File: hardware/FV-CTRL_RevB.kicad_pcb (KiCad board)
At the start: 2 copper layers, 100 x 100 mm, 152 parts, among them J1 12V INPUT, J10 IR RX2 3V3/OUT/G, J11 IR TX1 A/K, J12 IR TX2 A/K, J13 LS1 DNP, J14 LS2 DNP, J15 LS3 DNP, J16 LS4 DNP, J17 I2C 3V3/SDA/SCL/G, J2 XL4015 A: 12/G/6/G, J20 SMA 50ohm ANT, J21 USB MICRO DATA, J3 XL4015 B: 12/G/6/G, J4 5V D24V25F5, J5 S1_TOP, J6 S1_BOT, J7 S2_TOP, J8 S2_BOT, J9 IR RX1 3V3/OUT/G, Q1 IRF4905PBF, Q2 P2N2222AG, Q3 MMBT3904, Q4 MMBT3904, SW1 RESET, SW2 BOOT, U1 ESP32-D0WD-V3, U2 CP2102N-A02-GQFN24, U3 LD1117V33, U4 W25Q32JVSSIQ, U5 TLV803EA30DBZR, Y1 40MHz CL10pF

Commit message: feat(pcb): order QFN escapes and reconnect local supplies before signal routing
Keep two servo rails and GPIO unchanged. Use 0.4/0.2mm escape vias, move C23 to 0201 and preserve ground beneath clock/RF. ERC has zero violations; native DRC has no physical errors or parity differences, with 100 opens and 33 dangling warnings at this intermediate checkpoint. Not a fabrication release.
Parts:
- C23: footprint Capacitor_SMD:C_0402_1005Metric -> Capacitor_SMD:C_0201_0603Metric
- moved U5 10.0 mm to (135.0, 166.0)
- moved C56 4.47 mm to (138.0, 164.5)
- moved C13 4.29 mm to (142.0, 162.8), turned to -90 degrees
- moved C17 4.11 mm to (142.6, 159.8), turned to -90 degrees
- moved C18 2.77 mm to (149.0, 150.7), turned to 0 degrees
- moved C21 2.69 mm to (133.0, 157.5), turned to 90 degrees
- moved R40 2.50 mm to (150.5, 154.5)
- moved R41 2.50 mm to (150.5, 152.5)
- moved R42 2.50 mm to (152.5, 151.0)
- moved R43 2.50 mm to (154.5, 152.5)
- moved R44 2.50 mm to (152.5, 156.0)
- moved R45 2.50 mm to (150.5, 158.0)
- moved C15 2.00 mm to (135.5, 157.0), turned to 180 degrees
- moved C14 1.87 mm to (135.7, 154.0)
- moved C40 1.70 mm to (149.0, 156.8), turned to 0 degrees
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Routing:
- net +3V3: track 296.6 -> 350.2 mm, vias 9 -> 13
- net CAP2: track 0.00 -> 6.15 mm, vias 0 -> 2
- net CAP1: track 0.00 -> 4.27 mm, vias 0 -> 1
- net +3V3_RF: track 13.2 -> 16.8 mm
- net ESP_S2_BOT_PWM: track 0.00 -> 2.99 mm, vias 0 -> 1
- net ESP_S1_TOP_PWM: track 0.00 -> 2.99 mm, vias 0 -> 1
- net LS1: track 0.00 -> 2.90 mm, vias 0 -> 1
- net SPARE_GPIO33: track 0.00 -> 2.74 mm, vias 0 -> 1
- net ESP_IR_TX: track 0.00 -> 2.68 mm, vias 0 -> 1
- net ESP_S1_BOT_PWM: track 0.00 -> 2.68 mm, vias 0 -> 1
- net LS4: track 0.00 -> 2.62 mm, vias 0 -> 1
- net ESP_EN: track 0.00 -> 2.62 mm, vias 0 -> 1
- net IR_RX2: track 0.00 -> 2.56 mm, vias 0 -> 1
- net IR_RX1: track 0.00 -> 2.56 mm, vias 0 -> 1
- net SPI_HD: track 0.00 -> 2.56 mm, vias 0 -> 1
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
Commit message: feat(pcb): complete RevB routing, ground returns and service markings
Finish signal and supply connections, repair USB escape and C40 ground, and remove 24 redundant copper items. Apply 1mm/0.15mm silk rules, 0.025mm mask expansion and 0.10mm minimum mask web. Native KiCad ERC/DRC, opens and schematic parity are all zero. RF, thermal and hardware qualification remain pending; no Gerber release.
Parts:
- moved C40 4.57 mm to (145.0, 159.0), turned to 180 degrees
- moved C27 3.91 mm to (137.0, 146.0)
- moved C53 0.50 mm to (139.5, 183.8)
- moved C55 0.20 mm to (141.8, 188.4)
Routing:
- net LS2: track 2.08 -> 147.8 mm, vias 1 -> 10
- net LS3: track 1.89 -> 134.4 mm, vias 1 -> 0
- net LS1: track 2.90 -> 126.8 mm, vias 1 -> 10
- net LS4: track 2.62 -> 125.7 mm
- net I2C_SDA: track 1.78 -> 103.7 mm, vias 1 -> 3
- net I2C_SCL: track 2.14 -> 103.8 mm, vias 1 -> 2
- net ESP_EN: track 2.62 -> 102.0 mm, vias 1 -> 6
- net ESP_BOOT: track 1.84 -> 83.1 mm, vias 1 -> 4
- net UART_RX: track 1.99 -> 67.7 mm, vias 1 -> 4
- net ESP_IR_TX: track 2.68 -> 63.4 mm, vias 1 -> 2
- net IR_TX2_A: track 0.00 -> 58.8 mm
- net IR_TX_RET: track 0.00 -> 56.4 mm
- net IR_RX1: track 2.56 -> 58.8 mm, vias 1 -> 2
- net ESP_S2_BOT_PWM: track 2.99 -> 55.2 mm
- net UART_TX_RAW: track 1.86 -> 49.0 mm, vias 1 -> 6
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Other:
- rule pad_to_mask_clearance: 0 -> 0.025
- board text added: "12"
- board text added: "12V"
- board text added: "12V IN"
- board text added: "2026-10-20"
- board text added: "3V"
- board text added: "3V3"
- board text added: "5V"
- board text added: "5V LOGIC"
- board text added: "6A"
- board text added: "6B"
- board text added: "6V_A"
- board text added: "6V_B"
- board text added: "A"
- board text added: "ANT SMA"
- board text added: "BOOT"
- board text added: "BUCK A"
- board text added: "BUCK B"
- board text added: "EN"
- board text added: "FV-CTRL RevB"
- board text added: "G"
- board text added: "GND"
- board text added: "IO33"
- board text added: "J10 RX2"
- board text added: "J11 TX1"
- board text added: "J12 TX2"
- board text added: "J9 RX1"
- board text added: "K"
- board text added: "LS1 DNP"
- board text added: "LS2 DNP"
- board text added: "LS3 DNP"
- board text added: "LS4 DNP"
- board text added: "O"
- board text added: "RESET"
- board text added: "RX"
- board text added: "S"
- board text added: "S1 BOT"
- board text added: "S1 TOP"
- board text added: "S2 BOT"
- board text added: "S2 TOP"
- board text added: "SCL"
- board text added: "SDA"
- board text added: "TX"
- board text added: "USB DATA"
- board text added: "USB: 12V ON"

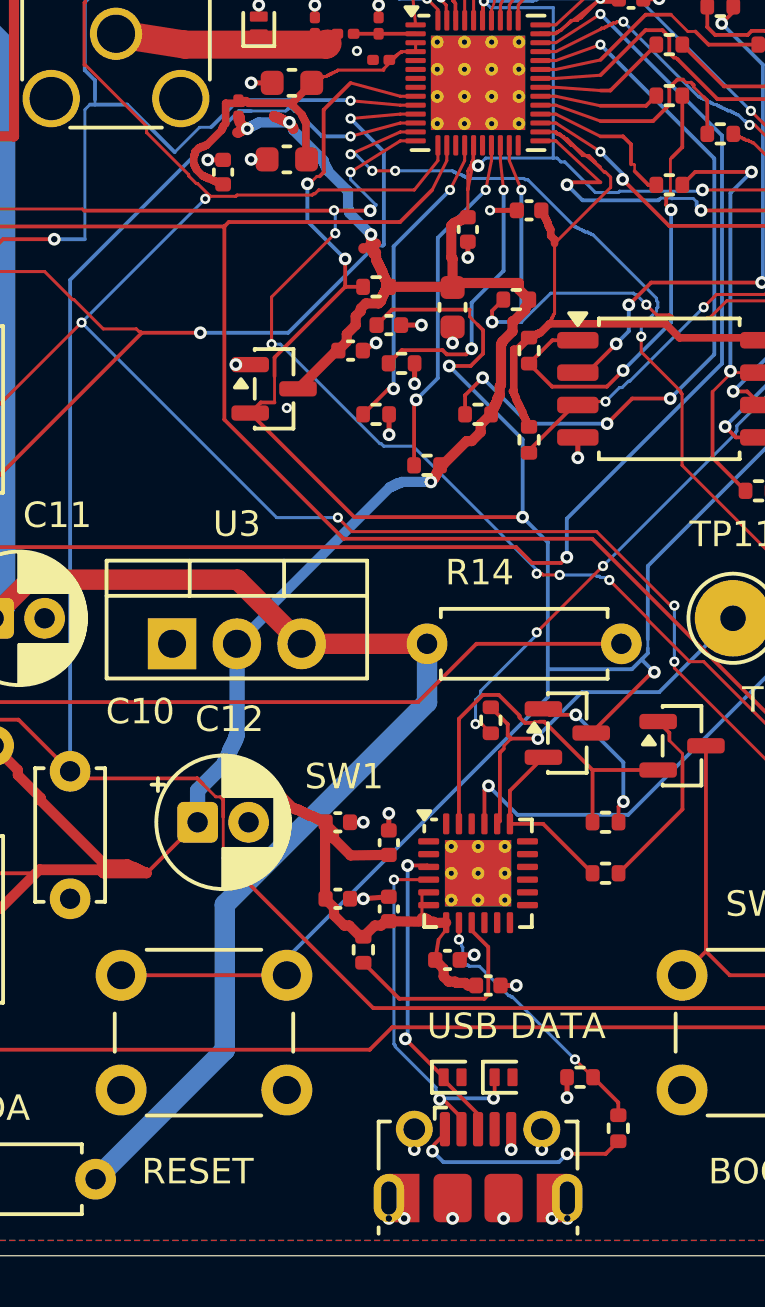
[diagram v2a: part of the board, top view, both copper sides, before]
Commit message: fix(pcb): keep ordinary ground drills outside SMT mask openings
Move USB shield/pin-5 and supervisor ground vias outside reflow openings. Use 0.4/0.2mm ground vias at C13/C15. Supplement native ERC/DRC with a conservative drill-to-mask check: minimum 0.05mm geometric guard, excluding thermal EP holes that require factory review. All software checks pass.
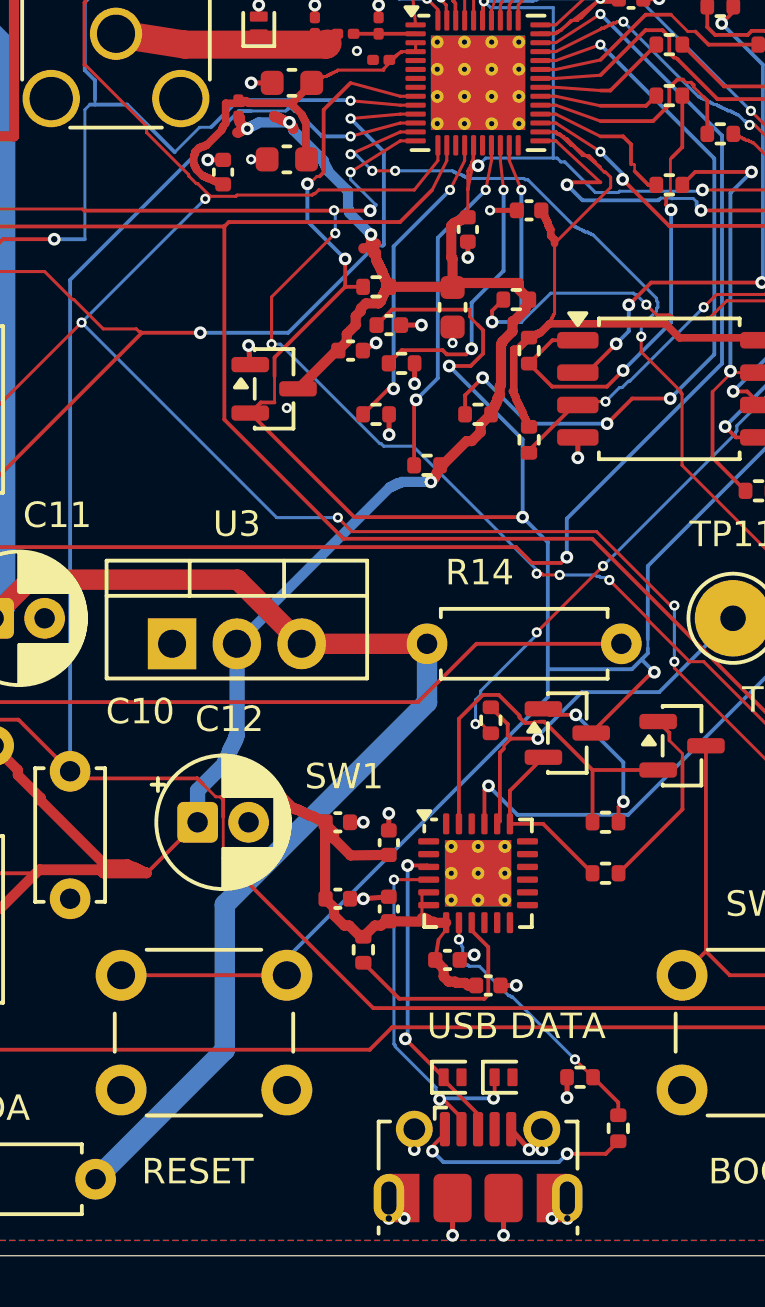
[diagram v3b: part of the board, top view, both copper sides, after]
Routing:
- net GND: track 28.6 -> 30.4 mm
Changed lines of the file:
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@@
 	(segment
 		(start 142 197.738)
-		(end 142 198.538)
+		(end 142 199.2)
 		(width 0.2)
 		(layer "F.Cu")
@@
 	(segment
 		(start 134.0625 165.05)
-		(end 133.5 165.05)
+		(end 134 164.3)
 		(width 0.2)
 		(layer "F.Cu")
@@
 	(segment
 		(start 144 197.738)
-		(end 144 198.538)
+		(end 144 199.2)
 		(width 0.2)
 		(layer "F.Cu")
@@
 	(segment
 		(start 144.3 195.038)
-		(end 144.3 195.838)
+		(end 145 195.838)
 		(width 0.2)
 		(layer "F.Cu")
@@
 	)
 	(via
-		(at 144 198.538)
+		(at 144 199.2)
 		(size 0.5)
 		(drill 0.25)
@@
 	(via
 		(at 142 164.2)
-		(size 0.5)
-		(drill 0.25)
+		(size 0.4)
+		(drill 0.2)
 		(layers "F.Cu" "B.Cu")
 		(net "GND")
@@
 	(via
 		(at 134.1 157)
-		(size 0.5)
-		(drill 0.25)
+		(size 0.4)
+		(drill 0.2)
 		(layers "F.Cu" "B.Cu")
 		(net "GND")
@@
 	)
 	(via
-		(at 144.3 195.838)
+		(at 145 195.838)
 		(size 0.5)
 		(drill 0.25)
@@
 	)
 	(via
-		(at 133.5 165.05)
-		(size 0.5)
-		(drill 0.25)
-		(layers "F.Cu" "B.Cu")
-		(net "GND")
-	)
-	(via
-		(at 142 198.538)
-		(size 0.5)
-		(drill 0.25)
+		(at 134 164.3)
+		(size 0.5)
+		(drill 0.25)
+		(layers "F.Cu" "B.Cu")
+		(net "GND")
+	)
+	(via
+		(at 142 199.2)
+		(size 0.5)
+		(drill 0.25)
